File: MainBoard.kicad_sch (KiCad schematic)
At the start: 4 parts, among them J1 Conn_01x06, J10 Conn_01x02, J2 Conn_01x06, U17 NUC_Buck

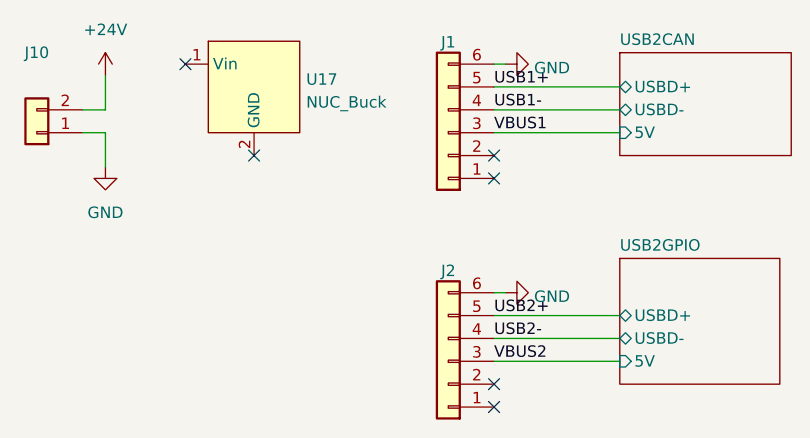
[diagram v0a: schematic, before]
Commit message: Change routings&Add ESD for UART and CAN&Add 5V protection and pull-resistance for GPIO
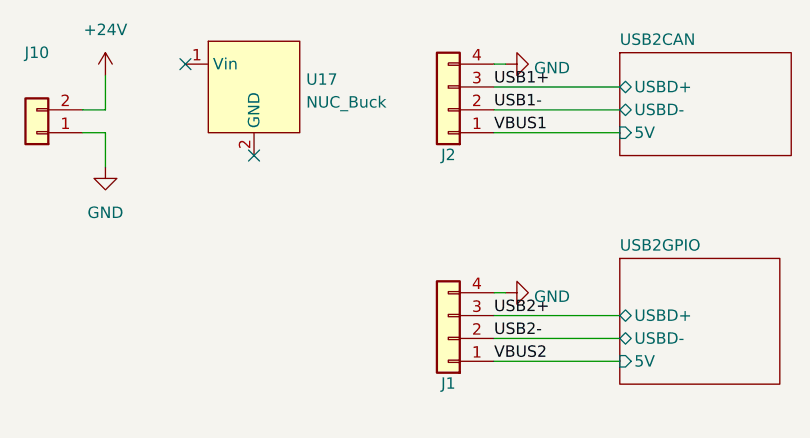
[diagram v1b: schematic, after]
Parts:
- removed J1, J2: Conn_01x06, Connector_FFC-FPC:Hirose_FH12-6S-0.5SH_1x06-1MP_P0.50mm_Horizontal, symbol Connector_Generic:Conn_01x06
- added J1, J2: Conn_01x04, Connector_Molex:Molex_CLIK-Mate_502386-0470_1x04-1MP_P1.25mm_Horizontal, symbol Connector_Generic:Conn_01x04
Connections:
- net GND: now also J1.4 (Pin_4), J2.4 (Pin_4)
- net USB1+: now also J2.3 (Pin_3)
- net USB1-: now also J2.2 (Pin_2)
- net USB2+: now also J1.3 (Pin_3)
- net USB2-: now also J1.2 (Pin_2)
- net VBUS1: now also J2.1 (Pin_1)
- net VBUS2: now also J1.1 (Pin_1)
- no-connect marks 6 -> 2
